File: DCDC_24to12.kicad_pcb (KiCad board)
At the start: 2 copper layers, 75 x 74.4 mm, 28 parts, among them J1 Power_IN, J2 Power_OUT, U1 BD9F800MUX-ZE2

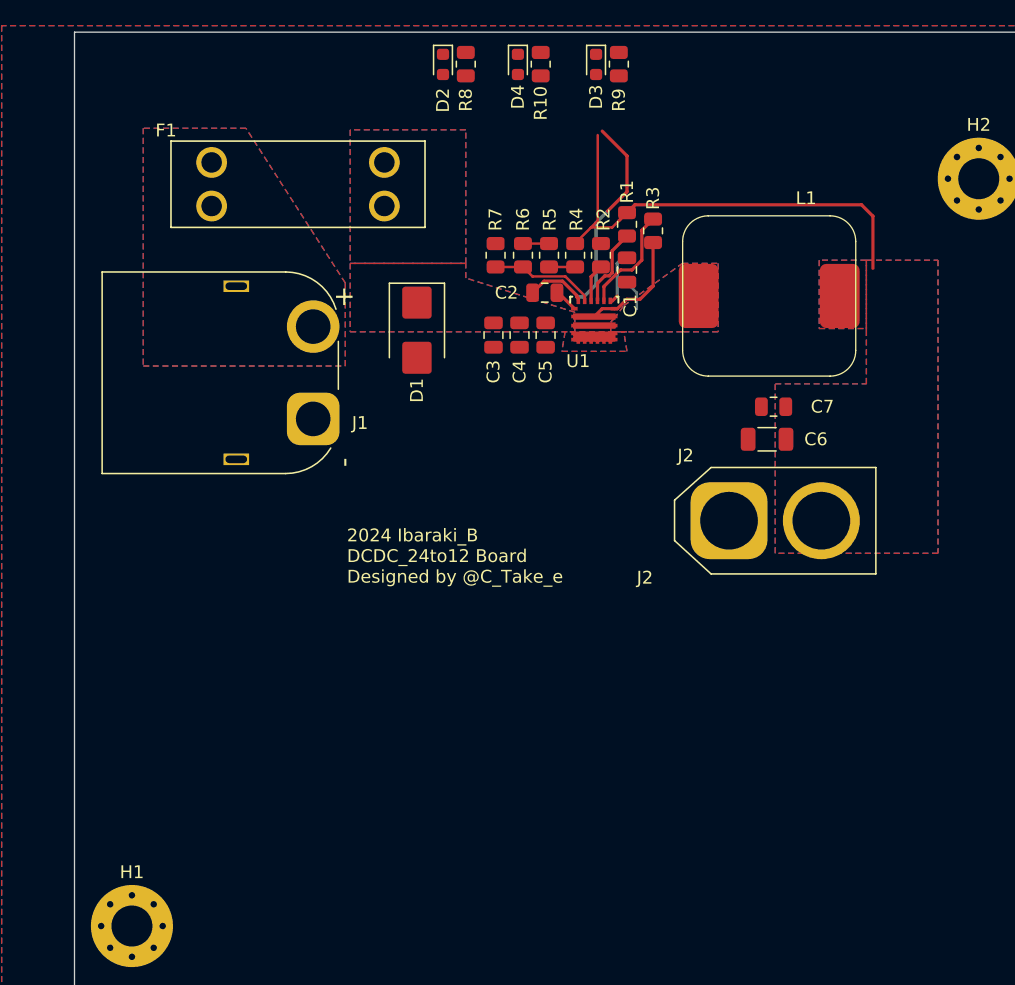
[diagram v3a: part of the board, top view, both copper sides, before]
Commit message: 抵抗の位置いろいろ変更 配線済み
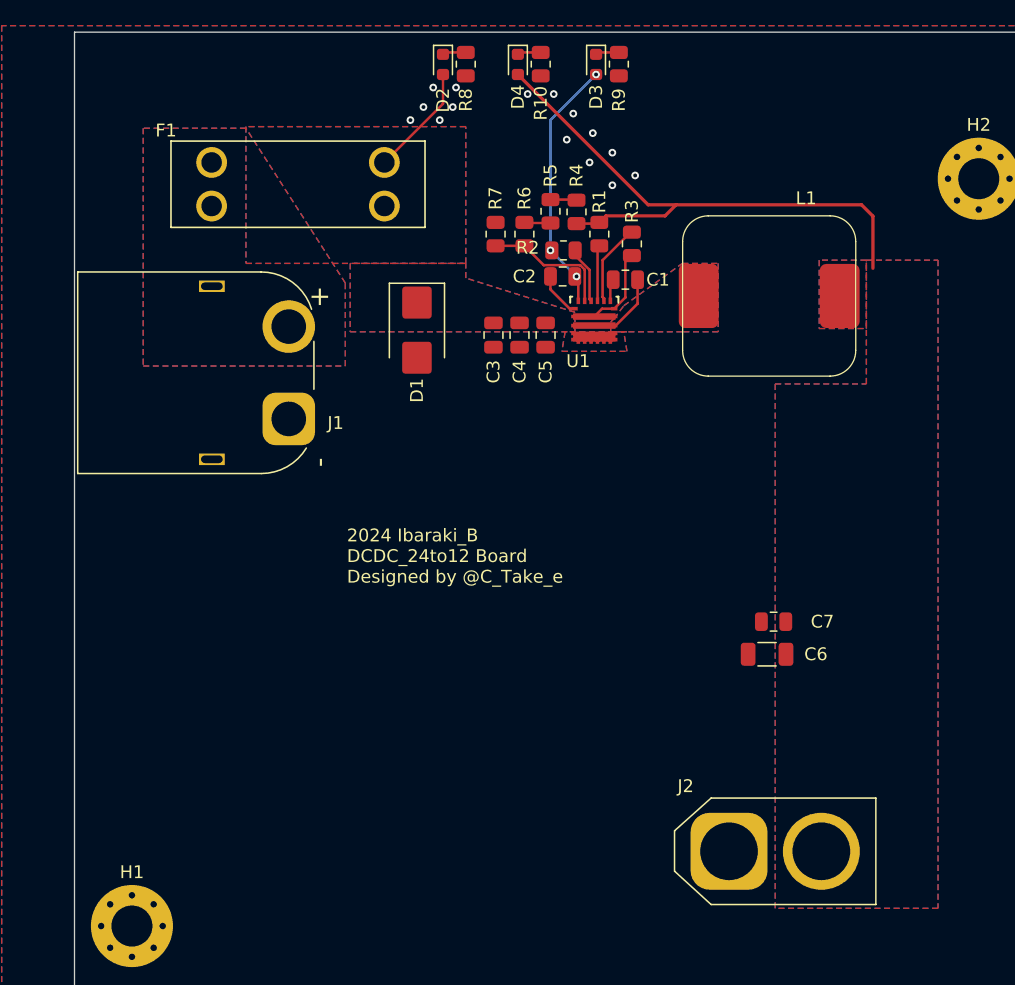
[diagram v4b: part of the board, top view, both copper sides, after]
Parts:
- moved J2 25.8 mm to (157.7, 136.3)
- moved C7 16.8 mm to (161.2, 118.4)
- moved C6 16.8 mm to (160.7, 120.9)
- moved R5 3.43 mm to (143.8, 86.4), turned to 90 degrees
- moved R4 3.38 mm to (145.8, 86.4), turned to -90 degrees
- moved R2 2.95 mm to (144.8, 89.4), turned to 180 degrees
- moved R1 2.29 mm to (147.6, 88.1)
- moved R3 1.94 mm to (150.1, 88.9)
- moved J1 1.91 mm to (123.4, 102.6)
- moved C2 1.89 mm to (144.7, 91.4), turned to 0 degrees
- moved R6 1.65 mm to (141.7, 88.1)
- moved R7 1.65 mm to (139.5, 88.1)
- moved C1 0.77 mm to (149.6, 91.7), turned to 0 degrees
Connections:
- net Net-(U1-FREQ) renamed FREQ
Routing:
- net +12V: track 36.3 -> 44.7 mm
- net +BATT: track 8.97 -> 15.4 mm
- net SW: track 2.35 -> 5.95 mm
- net BOOT: track 4.18 -> 1.74 mm
- net PGD: track 8.48 -> 6.41 mm
- net FB: track 8.28 -> 10.2 mm
- net Net-(U1-VOUT): track 6.20 -> 4.35 mm
- net Net-(D4-K): track 0.00 -> 1.84 mm
- net Net-(D3-K): track 0.00 -> 1.84 mm
- net Net-(D2-K): track 0.00 -> 1.84 mm
- net FREQ: track 2.98 -> 4.45 mm
- net GND: track 2.73 -> 3.63 mm, vias 0 -> 15
- net VREG: track 20.4 -> 20.2 mm, vias 0 -> 3
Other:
- board text removed: "J2"

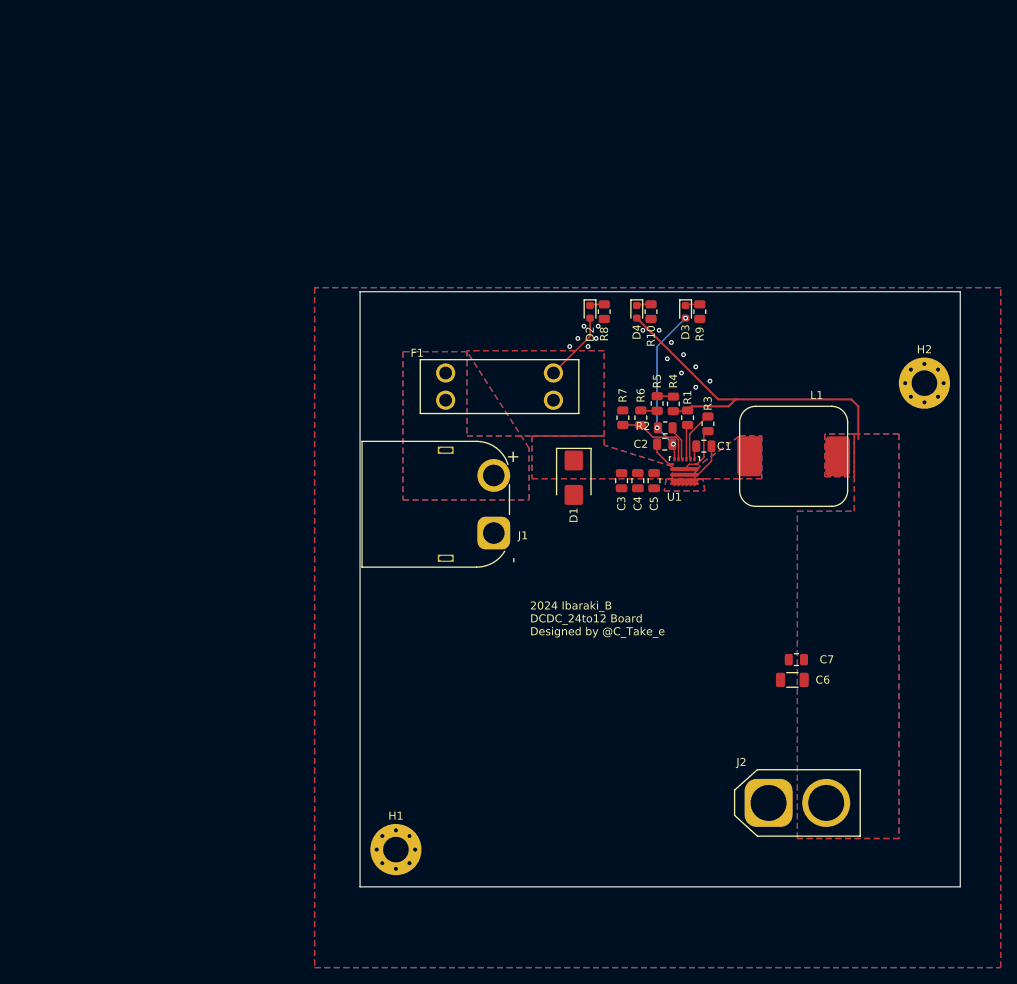
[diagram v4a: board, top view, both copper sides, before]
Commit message: GND回り込み経路を修正
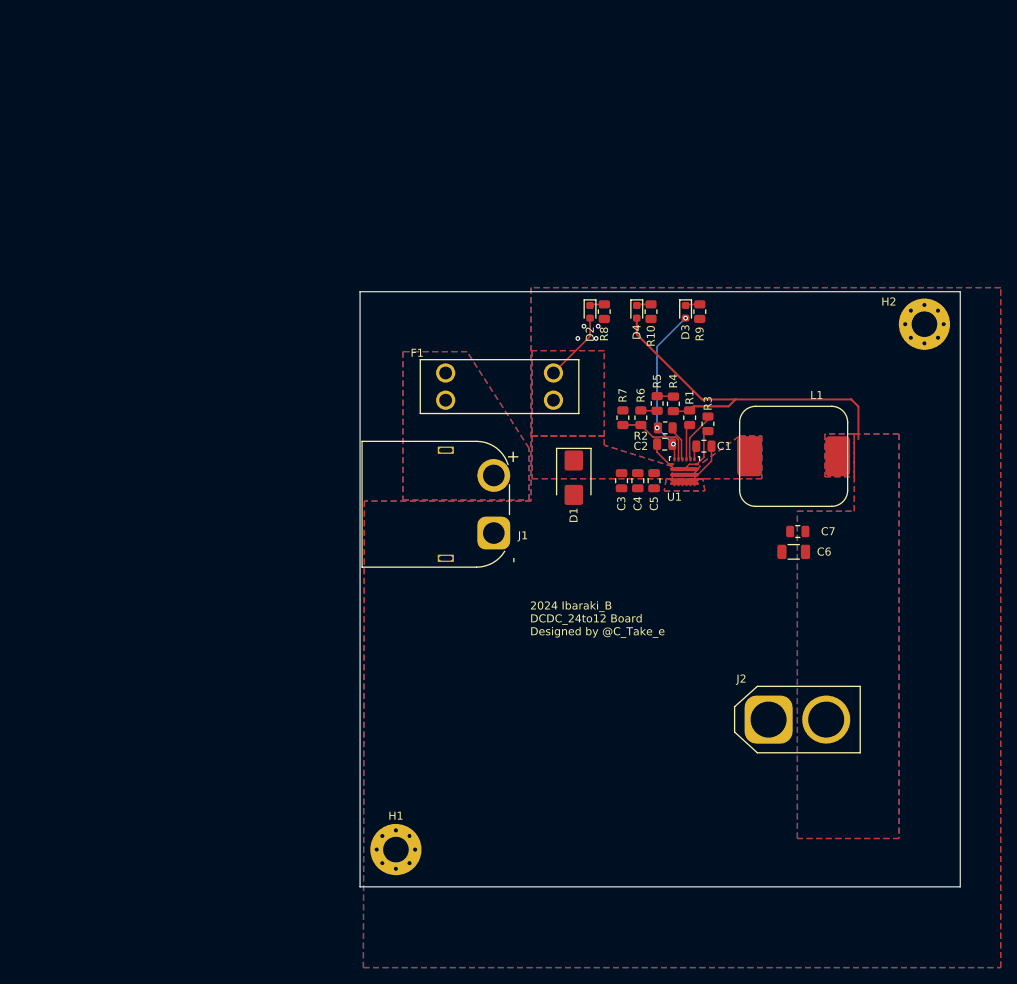
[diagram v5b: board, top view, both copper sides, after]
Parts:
- moved C7 16.0 mm to (161.3, 102.4)
- moved C6 16.0 mm to (160.8, 104.9)
- moved J2 10.4 mm to (157.7, 125.9)
- moved H2 7.37 mm to (177.2, 76.5)
- moved R1 0.25 mm to (147.8, 88.1)
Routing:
- net +12V: track 44.7 -> 45.9 mm
- net GND: vias 15 -> 4
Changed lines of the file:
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@@
 	(footprint "Capacitor_SMD:C_0805_2012Metric"
 		(layer "F.Cu")
-		(at 161.163 118.364 180)
+		(at 161.339 102.362 180)
 		(descr "Capacitor SMD 0805 (2012 Metric), square (rectangular) end terminal, IPC_7351 nominal, (Body size source: IPC-SM-782 page 76, https://www.pcb-3d.com/wordpress/wp-content/uploads/ipc-sm-782a_amendment_1_and_2.pdf, https://docs.google.com/spreadsheets/d/1BsfQQcO9C6DZCsRaXUlFlo91Tg2WpOkGARC1WS5S8t0/edit?usp=sharing), generated with kicad-footprint-generator")
 		(tags "capacitor")
@@
 	(footprint "MountingHole:MountingHole_3.2mm_M3_Pad_Via"
 		(layer "F.Cu")
-		(at 177.165 83.82)
+		(at 177.165 76.454)
 		(descr "Mounting Hole 3.2mm, M3")
 		(tags "mounting hole 3.2mm m3")
 		(property "Reference" "H2"
-			(at 0 -4.2 0)
+			(at -4.445 -2.794 0)
 			(layer "F.SilkS")
 			(effects
@@
 	(footprint "Capacitor_SMD:C_1206_3216Metric"
 		(layer "F.Cu")
-		(at 160.655 120.904 180)
+		(at 160.831 104.902 180)
 		(descr "Capacitor SMD 1206 (3216 Metric), square (rectangular) end terminal, IPC_7351 nominal, (Body size source: IPC-SM-782 page 76, https://www.pcb-3d.com/wordpress/wp-content/uploads/ipc-sm-782a_amendment_1_and_2.pdf), generated with kicad-footprint-generator")
 		(tags "capacitor")
@@
 	(footprint "Resistor_SMD:R_0805_2012Metric"
 		(layer "F.Cu")
-		(at 147.574 88.138 -90)
+		(at 147.828 88.138 -90)
 		(descr "Resistor SMD 0805 (2012 Metric), square (rectangular) end terminal, IPC_7351 nominal, (Body size source: IPC-SM-782 page 72, https://www.pcb-3d.com/wordpress/wp-content/uploads/ipc-sm-782a_amendment_1_and_2.pdf), generated with kicad-footprint-generator")
 		(tags "resistor")
@@
 		(tags "capacitor")
 		(property "Reference" "C2"
-			(at -2.981999 0 360)
+			(at -2.981999 0.254 360)
 			(layer "F.SilkS")
 			(effects
@@
 	(footprint "Connector_AMASS:AMASS_XT60-F_1x02_P7.20mm_Vertical"
 		(layer "F.Cu")
-		(at 157.69 136.271)
+		(at 157.69 125.857)
 		(descr "AMASS female XT60, through hole, vertical, https://www.tme.eu/Document/2d152ced3b7a446066e6c419d84bb460/XT60%20SPEC.pdf")
 		(tags "XT60 female vertical")
@@
 		(tags "resistor")
 		(property "Reference" "R2"
-			(at 2.794 0.2032 360)
+			(at 3.048 -1.016 360)
 			(layer "F.SilkS")
 			(effects
@@
 	)
 	(gr_rect
-		(start 153.924 132.588)
-		(end 160.909 140.208)
+		(start 153.924 122.174)
+		(end 160.909 129.794)
 		(stroke
 			(width 0.1)
@@
 	)
 	(gr_rect
-		(start 161.798 132.461)
-		(end 168.783 140.208)
+		(start 161.798 122.047)
+		(end 168.783 129.794)
 		(stroke
 			(width 0.1)
@@
 	)
 	(via
-		(at 132.842 79.248)
-		(size 0.6)
-		(drill 0.3)
-		(layers "F.Cu" "B.Cu")
-		(free yes)
-		(net 1)
-	)
-	(via
-		(at 141.986 77.216)
-		(size 0.6)
-		(drill 0.3)
-		(layers "F.Cu" "B.Cu")
-		(free yes)
-		(net 1)
-	)
-	(via
 		(at 136.398 76.708)
 		(size 0.6)
@@
 	)
 	(via
-		(at 135.128 79.248)
-		(size 0.6)
-		(drill 0.3)
-		(layers "F.Cu" "B.Cu")
-		(free yes)
-		(net 1)
-	)
-	(via
 		(at 134.62 76.708)
 		(size 0.6)
@@
 	)
 	(via
-		(at 148.59 81.788)
-		(size 0.6)
-		(drill 0.3)
-		(layers "F.Cu" "B.Cu")
-		(free yes)
-		(net 1)
-	)
-	(via
-		(at 145.034 80.772)
-		(size 0.6)
-		(drill 0.3)
-		(layers "F.Cu" "B.Cu")
-		(free yes)
-		(net 1)
-	)
-	(via
-		(at 144.018 77.216)
-		(size 0.6)
-		(drill 0.3)
-		(layers "F.Cu" "B.Cu")
-		(free yes)
-		(net 1)
-	)
-	(via
-		(at 146.812 82.55)
-		(size 0.6)
-		(drill 0.3)
-		(layers "F.Cu" "B.Cu")
-		(free yes)
-		(net 1)
-	)
-	(via
-		(at 150.368 83.566)
-		(size 0.6)
-		(drill 0.3)
-		(layers "F.Cu" "B.Cu")
-		(free yes)
-		(net 1)
-	)
-	(via
 		(at 133.858 78.232)
 		(size 0.6)
@@
 	)
 	(via
-		(at 148.59 84.328)
-		(size 0.6)
-		(drill 0.3)
-		(layers "F.Cu" "B.Cu")
-		(free yes)
-		(net 1)
-	)
-	(via
-		(at 147.066 80.264)
-		(size 0.6)
-		(drill 0.3)
-		(layers "F.Cu" "B.Cu")
-		(free yes)
-		(net 1)
-	)
-	(via
 		(at 136.144 78.232)
 		(size 0.6)
@@
 		(net 1)
 	)
-	(via
-		(at 145.542 78.74)
-		(size 0.6)
-		(drill 0.3)
-		(layers "F.Cu" "B.Cu")
-		(free yes)
-		(net 1)
-	)
 	(segment
 		(start 168.91 86.741)
@@
 	)
 	(segment
-		(start 168.021 85.852)
-		(end 168.91 86.741)
+		(start 149.368709 85.852)
+		(end 141.224 77.707291)
 		(width 0.254)
 		(layer "F.Cu")
@@
 	)
 	(segment
-		(start 151.384 85.852)
-		(end 141.224 75.692)
+		(start 148.336 86.7175)
+		(end 152.701 86.7175)
 		(width 0.254)
 		(layer "F.Cu")
@@
 	(segment
 		(start 145.796 87.3195)
-		(end 147.48 87.3195)
+		(end 147.734 87.3195)
 		(width 0.2)
 		(layer "F.Cu")
@@
 	)
 	(segment
-		(start 152.701 86.7175)
-		(end 153.5665 85.852)
+		(start 147.734 87.3195)
+		(end 147.828 87.2255)
+		(width 0.2)
+		(layer "F.Cu")
+		(net 2)
+	)
+	(segment
+		(start 168.021 85.852)
+		(end 168.91 86.741)
 		(width 0.254)
 		(layer "F.Cu")
@@
 	)
 	(segment
-		(start 147.48 87.3195)
-		(end 147.574 87.2255)
-		(width 0.2)
+		(start 152.701 86.7175)
+		(end 153.5665 85.852)
+		(width 0.254)
 		(layer "F.Cu")
 		(net 2)
 	)
 	(segment
-		(start 153.5665 85.852)
-		(end 151.384 85.852)
+		(start 147.828 87.2255)
+		(end 148.336 86.7175)
 		(width 0.254)
 		(layer "F.Cu")
@@
 	)
 	(segment
-		(start 148.082 86.7175)
-		(end 152.701 86.7175)
+		(start 153.5665 85.852)
+		(end 149.368709 85.852)
 		(width 0.254)
 		(layer "F.Cu")
@@
 	)
 	(segment
-		(start 147.574 87.2255)
-		(end 148.082 86.7175)
+		(start 141.224 77.707291)
+		(end 141.224 75.692)
 		(width 0.254)
 		(layer "F.Cu")
@@
 	)
 	(segment
-		(start 147.433063 93.345)
-		(end 147.433063 89.191437)
+		(start 147.433063 89.445437)
+		(end 147.828 89.0505)
 		(width 0.2)
 		(layer "F.Cu")
@@
 	)
 	(segment
-		(start 147.433063 89.191437)
-		(end 147.574 89.0505)
+		(start 147.433063 93.345)
+		(end 147.433063 89.445437)
 		(width 0.2)
 		(layer "F.Cu")
@@
 	)
 	(segment
-		(start 150.114 87.9875)
-		(end 150.014446 87.9875)
+		(start 147.933189 93.151426)
+		(end 147.933189 93.345)
 		(width 0.2)
 		(layer "F.Cu")
@@
 	)
 	(segment
-		(start 147.828 90.173946)
+		(start 147.828 90.678)
 		(end 147.828 93.046237)
 		(width 0.2)
@@
 	)
 	(segment
-		(start 150.014446 87.9875)
-		(end 147.828 90.173946)
+		(start 147.828 93.046237)
+		(end 147.933189 93.151426)
 		(width 0.2)
 		(layer "F.Cu")
@@
 	)
 	(segment
-		(start 147.933189 93.151426)
-		(end 147.933189 93.345)
+		(start 150.114 87.9875)
+		(end 150.114 88.392)
 		(width 0.2)
 		(layer "F.Cu")
@@
 	)
 	(segment
-		(start 147.828 93.046237)
-		(end 147.933189 93.151426)
+		(start 150.114 88.392)
+		(end 147.828 90.678)
 		(width 0.2)
 		(layer "F.Cu")
@@
 		(polygon
 			(pts
-				(xy 100.965 71.882) (xy 100.965 156.845) (xy 186.69 156.845) (xy 186.69 71.882)
+				(xy 128.016 71.882) (xy 128.016 98.552) (xy 107.188 98.552) (xy 107.061 156.845) (xy 186.69 156.845)
+				(xy 186.69 71.882)
 			)
 		)
@@
 		(polygon
 			(pts
-				(xy 120.015 79.756) (xy 120.015 90.424) (xy 137.16 90.424) (xy 137.16 79.756)
+				(xy 128.143 79.756) (xy 128.143 90.424) (xy 137.16 90.424) (xy 137.16 79.756)
 			)
 		)

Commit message: 4層になりました
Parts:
- moved J2 14.1 mm to (157.7, 111.8)
- moved H2 0.51 mm to (177.2, 77.0)
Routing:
- net +12V: track 45.9 -> 47.9 mm, vias 0 -> 17
- net SW: vias 0 -> 12
- added copper zone on In1.Cu, net +12V
- added copper zone on In2.Cu, net +12V
- added copper zone on In1.Cu, net +BATT
- added copper zone on In2.Cu, net +BATT
- added copper zone on In1.Cu, net GND
- added copper zone on In2.Cu, net GND
- added copper zone on In1.Cu, net Net-(J1-Pin_2)
- added copper zone on In2.Cu, net Net-(J1-Pin_2)
- added copper zone on In1.Cu, net SW
- added copper zone on In2.Cu, net SW
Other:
- copper layers 2 -> 4

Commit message: 集合体恐怖症絶対ビビらせるビア
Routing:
- net GND: vias 4 -> 340
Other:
- board text added: "${REFERENCE}"
